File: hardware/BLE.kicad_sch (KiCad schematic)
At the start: 0 parts

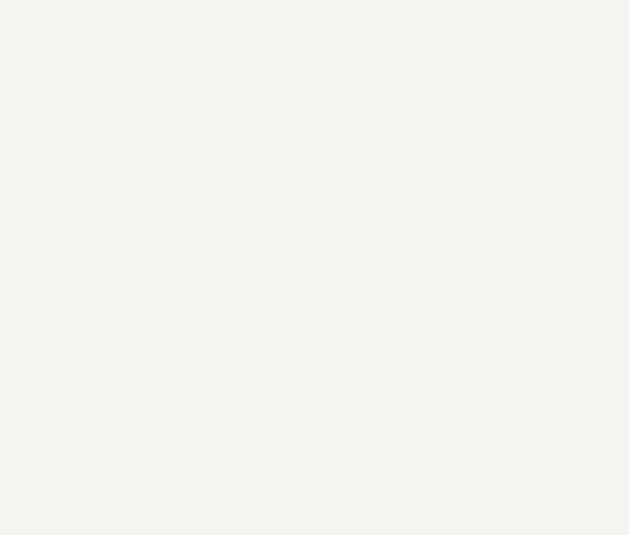
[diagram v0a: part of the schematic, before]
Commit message: Schematic updates: stm32 sheet
Signed-off-by: Connor Rigby <connorr@hey.com>
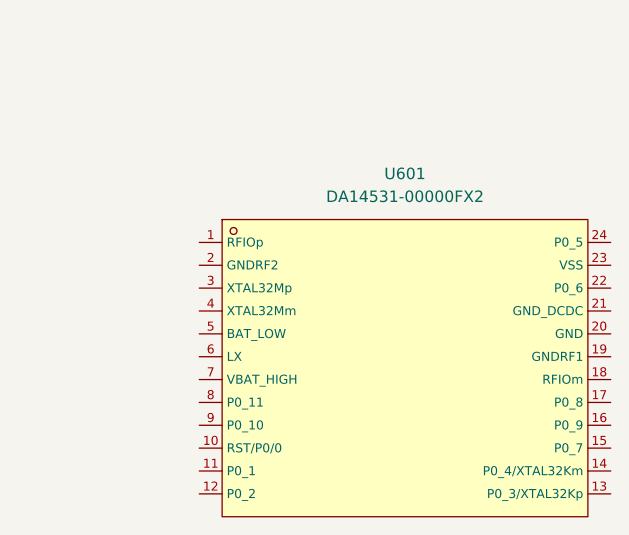
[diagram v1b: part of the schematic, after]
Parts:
- added U601: DA14531-00000FX2, LCSC_Microcontroller:FCGQFN-24_L3.0-W2.2-P0.40-BL, symbol LCSC_Microcontroller:DA14531-00000FX2
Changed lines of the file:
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@@
     (effects (font (size 1.27 1.27)) (justify left))
   )
+  (symbol (lib_id "LCSC_Microcontroller:DA14531-00000FX2") (at 124.46 77.47 0) (unit 1)
+    (in_bom yes) (on_board yes) (fields_autoplaced)
+    (property "Reference" "U601" (id 0) (at 124.46 55.88 0))
+    (property "Value" "DA14531-00000FX2" (id 1) (at 124.46 58.42 0))
+    (property "Footprint" "LCSC_Microcontroller:FCGQFN-24_L3.0-W2.2-P0.40-BL" (id 2) (at 124.46 74.93 0)
+      (effects (font (size 1.27 1.27) italic) hide)
+    )
+    (property "Datasheet" "https://datasheet.lcsc.com/lcsc/2004091707_Dialog-Semiconductor-DA14531-00000FX2_C509077.pdf" (id 3) (at 122.174 64.643 0)
+      (effects (font (size 1.27 1.27)) (justify left) hide)
+    )
+    (property "LCSC" "C509077" (id 4) (at 124.46 64.77 0)
+      (effects (font (size 1.27 1.27)) hide)
+    )
+    (property "MPN" "DA14531-00000FX2" (id 5) (at 124.46 64.77 0)
+      (effects (font (size 1.27 1.27)) hide)
+    )
+    (pin "1")
+    (pin "10")
+    (pin "11")
+    (pin "12")
+    (pin "13")
+    (pin "14")
+    (pin "15")
+    (pin "16")
+    (pin "17")
+    (pin "18")
+    (pin "19")
+    (pin "2")
+    (pin "20")
+    (pin "21")
+    (pin "22")
+    (pin "23")
+    (pin "24")
+    (pin "3")
+    (pin "4")
+    (pin "5")
+    (pin "6")
+    (pin "7")
+    (pin "8")
+    (pin "9")
+  )
 )

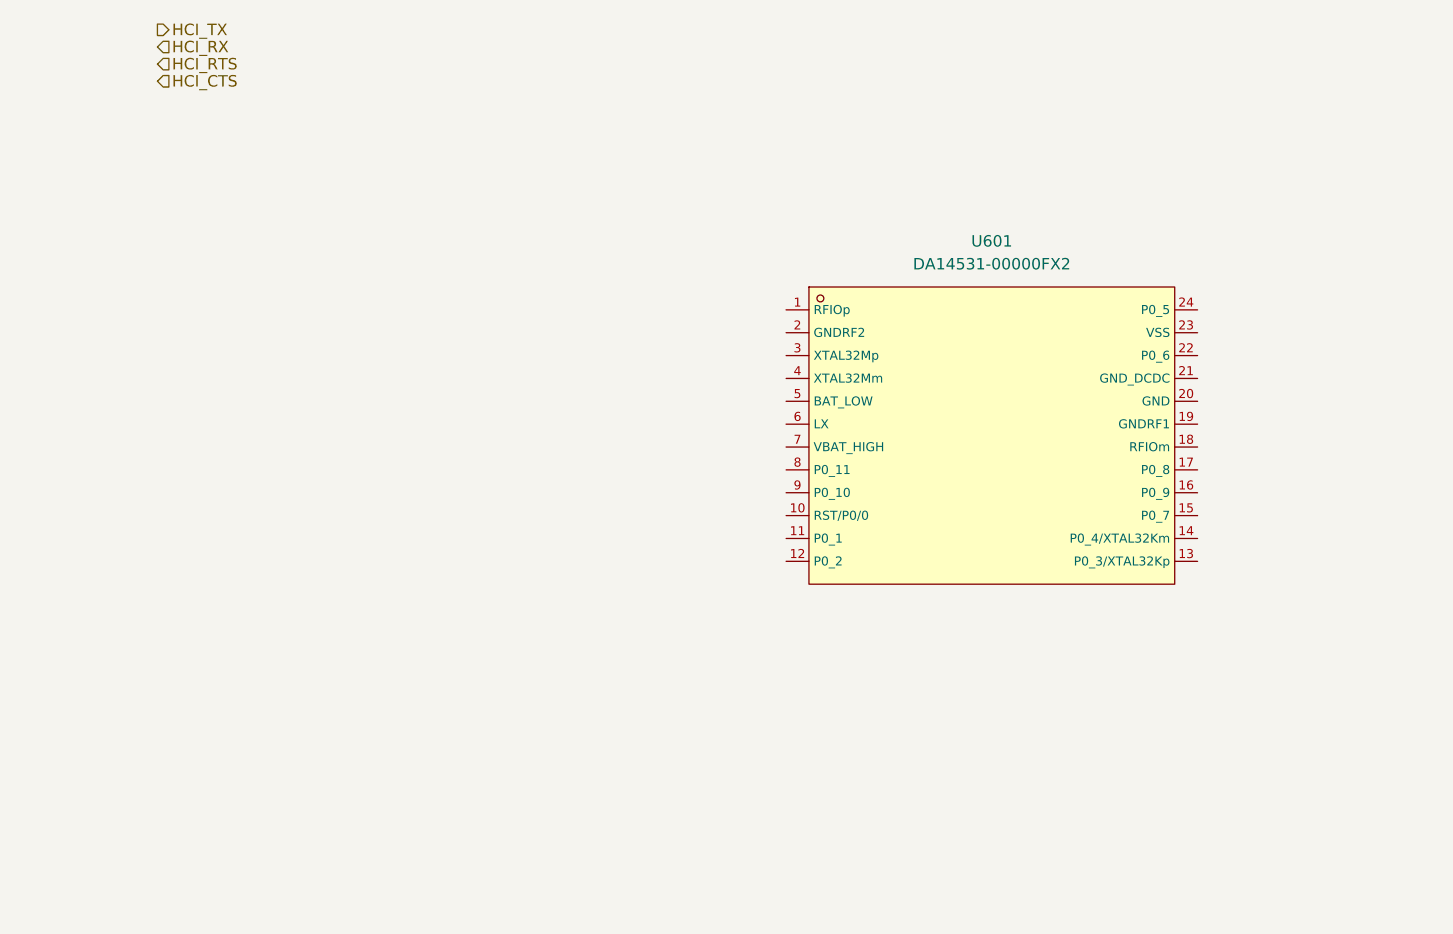
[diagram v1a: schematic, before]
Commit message: Schematic and layout Progress
Signed-off-by: Connor Rigby <connorr@hey.com>
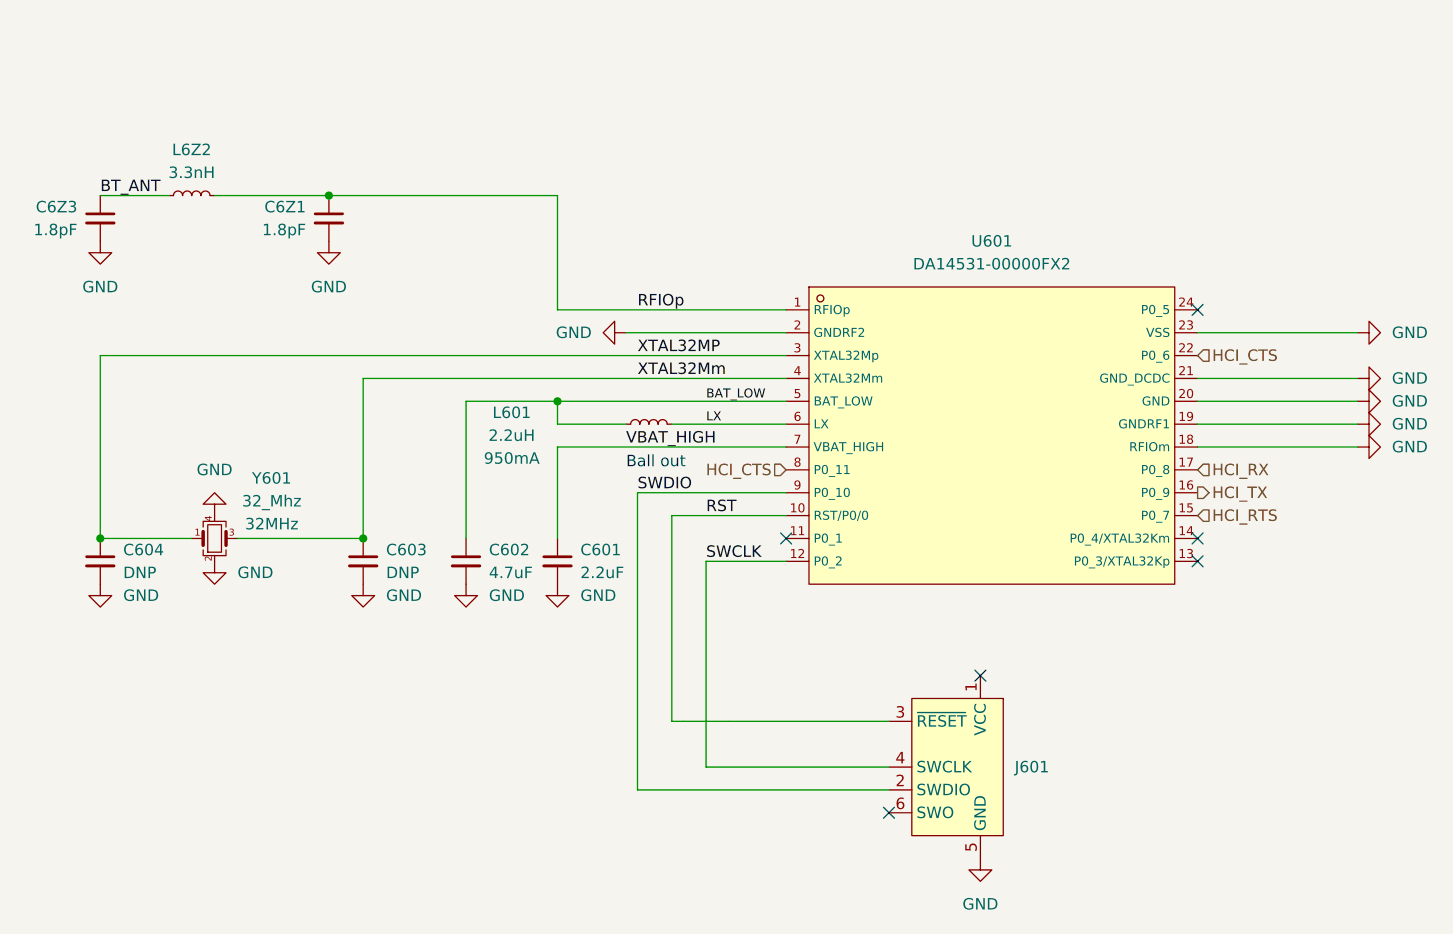
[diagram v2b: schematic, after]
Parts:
- added C601: C_0402_2u2_X75R, Capacitor_SMD:C_0402_1005Metric, symbol LCSC_Capacitor:C_0402_2u2_X75R
- added C602: C_0402_4u7_X5R, Capacitor_SMD:C_0402_1005Metric, symbol LCSC_Capacitor:C_0402_4u7_X5R
- added C603, C604: C_0402_DNP, Capacitor_SMD:C_0402_1005Metric, symbol LCSC_Capacitor:C_0402_DNP
- added C6Z1, C6Z3: C_0402_1p8_C0G, Capacitor_SMD:C_0402_1005Metric, symbol LCSC_Capacitor:C_0402_1p8_C0G
- added J601: Conn_ARM_SWD_TagConnect_TC2030-NL, Connector:Tag-Connect_TC2030-IDC-NL_2x03_P1.27mm_Vertical, symbol Connector:Conn_ARM_SWD_TagConnect_TC2030-NL
- added L601: L_0805_2u2, Inductor_SMD:L_0805_2012Metric, symbol LCSC_Power_Inductor:L_0805_2u2
- added L6Z2: L_0402_3n3, Inductor_SMD:L_0402_1005Metric, symbol LCSC_Inductor:L_0402_3n3
- added Y601: 32_Mhz, Crystal:Crystal_SMD_3225-4Pin_3.2x2.5mm, symbol LCSC_Crystal:32_Mhz
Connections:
- net HCI_CTS: now also U601.22 (P0_6), U601.8 (P0_11)
- net HCI_RTS: now also U601.15 (P0_7)
- net HCI_RX: now also U601.17 (P0_8)
- net HCI_TX: now also U601.16 (P0_9)
- net RFIOp: now reaches U601.1 (RFIOp)
- net RFIOp: now also C6Z1.1, L6Z2.1
- net RST: now reaches U601.10 (RST/P0/0)
- net RST: now also J601.3 (~{RESET})
- net SWCLK: now reaches U601.12 (P0_2)
- net SWCLK: now also J601.4 (SWCLK)
- net GND: now reaches U601.18 (RFIOm)
- net GND: now also U601.19 (GNDRF1), U601.2 (GNDRF2), U601.20 (GND), U601.21 (GND_DCDC), U601.23 (VSS), C601.2, C602.2, C603.2, C604.2, C6Z1.2, C6Z3.2, J601.5 (GND), Y601.2, Y601.4
- net XTAL32MP: now reaches U601.3 (XTAL32Mp)
- net XTAL32MP: now also C604.1, Y601.1
- net XTAL32Mm: now reaches U601.4 (XTAL32Mm)
- net XTAL32Mm: now also C603.1, Y601.3
- net BAT_LOW: now reaches U601.5 (BAT_LOW)
- net BAT_LOW: now also C602.1, L601.1
- net LX: now reaches U601.6 (LX)
- net LX: now also L601.2
- net VBAT_HIGH: now reaches U601.7 (VBAT_HIGH)
- net VBAT_HIGH: now also C601.1
- net SWDIO: now reaches U601.9 (P0_10)
- net SWDIO: now also J601.2 (SWDIO)
- new net BT_ANT: C6Z3.1, L6Z2.2
- no-connect marks 0 -> 6
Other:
- note added: "Ball out"

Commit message: Layout updates
Signed-off-by: Connor Rigby <connorr@hey.com>
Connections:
- net VBAT_HIGH renamed +3.3V
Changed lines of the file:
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@@
   (junction (at 50.8 50.8) (diameter 0) (color 0 0 0 0)
+  )
+  (junction (at 76.2 78.74) (diameter 0) (color 0 0 0 0)
   )
   (junction (at 54.61 88.9) (diameter 0) (color 0 0 0 0)
@@
     (stroke (width 0) (type default))
   )
+  (wire (pts (xy 71.12 78.74) (xy 76.2 78.74))
+    (stroke (width 0) (type default))
+  )
   (wire (pts (xy 85.09 116.84) (xy 113.03 116.84))
     (stroke (width 0) (type default))
@@
   )
   (label "SWDIO" (at 85.09 83.82 0) (fields_autoplaced)
-    (effects (font (size 1.27 1.27)) (justify left bottom))
-  )
-  (label "VBAT_HIGH" (at 83.82 78.74 0) (fields_autoplaced)
     (effects (font (size 1.27 1.27)) (justify left bottom))
   )
@@
   (symbol (lib_id "LCSC_Power_Inductor:L_0805_2u2") (at 86.36 76.2 90) (unit 1)
     (in_bom yes) (on_board yes) (dnp no)
-    (property "Reference" "L601" (at 71.12 74.93 90)
+    (property "Reference" "L601" (at 62.23 74.93 90)
       (effects (font (size 1.27 1.27)))
     )
@@
       (effects (font (size 1.27 1.27)) hide)
     )
-    (property "Inductance" "2.2uH" (at 71.12 77.47 90)
+    (property "Inductance" "2.2uH" (at 62.23 77.47 90)
       (effects (font (size 1.27 1.27)))
     )
@@
       (effects (font (size 1.27 1.27)) hide)
     )
-    (property "Current" "950mA" (at 71.12 80.01 90)
+    (property "Current" "950mA" (at 62.23 80.01 90)
       (effects (font (size 1.27 1.27)))
     )
@@
         )
       )
+    )
+  )
+  (symbol (lib_id "power:+3.3V") (at 71.12 78.74 0) (unit 1)
+    (in_bom yes) (on_board yes) (dnp no) (fields_autoplaced)
+    (property "Reference" "#PWR0601" (at 71.12 82.55 0)
+      (effects (font (size 1.27 1.27)) hide)
+    )
+    (property "Value" "+3.3V" (at 71.12 74.93 0)
+      (effects (font (size 1.27 1.27)))
+    )
+    (property "Footprint" "" (at 71.12 78.74 0)
+      (effects (font (size 1.27 1.27)) hide)
+    )
+    (property "Datasheet" "" (at 71.12 78.74 0)
+      (effects (font (size 1.27 1.27)) hide)
+    )
+    (pin "1")
+    (instances
+      (project "underglow2"
+        (path "/dcbdf88a-d6ac-4b1d-9514-0b0ce113d90b/f6dd0682-1649-403c-b931-941640049f3a"
+          (reference "#PWR0601") (unit 1)
+        )
+      )

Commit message: layout updates
Signed-off-by: Connor Rigby <connorr@hey.com>
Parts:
- added ANT601: BWIPX-1-001E, LCSC_Antenna:IPEX-SMD_BWIPX-1-001E, symbol LCSC_Antenna:BWIPX-1-001E
- added C826, C827: C_0402_DNP, Capacitor_SMD:C_0402_1005Metric, symbol LCSC_Capacitor:C_0402_DNP
- added R804: R_0402_DNP, Resistor_SMD:R_0402_1005Metric, symbol LCSC_Resistor:R_0402_DNP
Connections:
- net BT_ANT: now also C826.2, R804.1
- net GND: now also ANT601.2 (GND), ANT601.3 (GND), C826.1, C827.1
- new net: ANT601.1 (SIG), C827.2, R804.2

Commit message: Almost ready for fab
Signed-off-by: Connor Rigby <connorr@hey.com>
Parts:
- removed C603, C604: C_0402_DNP, Capacitor_SMD:C_0402_1005Metric, symbol LCSC_Capacitor:C_0402_DNP
- removed R804: R_0402_DNP, Resistor_SMD:R_0402_1005Metric, symbol LCSC_Resistor:R_0402_DNP
- added C603, C604: C_0402_33p_C0G, Capacitor_SMD:C_0402_1005Metric, symbol LCSC_Capacitor:C_0402_33p_C0G
- added R601: R_0402_0, Resistor_SMD:R_0402_1005Metric, symbol LCSC_Resistor:R_0402_0
- C826, C827: now not fitted
- J601: now left out of the parts list
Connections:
- net BT_ANT: now also R601.1
- net GND: now also C603.2, C604.2
- net XTAL32MP: now also C604.1
- net XTAL32Mm: now also C603.1
- net BLE_ANT: now reaches ANT601.1 (SIG), C827.2
- net BLE_ANT: now also R601.2

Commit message: Pre-production updates
Signed-off-by: Connor Rigby <connorr@hey.com>
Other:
- note removed: "Ball out"
- company: (none) -> https://cone.codes
- title: (none) -> coneRGB2
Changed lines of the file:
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@@
 (kicad_sch (version 20230121) (generator eeschema)
   (paper "A4")
+  (title_block
+    (title "coneRGB2")
+    (date "2023-03-20")
+    (rev "1")
+    (company "https://cone.codes")
+    (comment 1 "https://github.com/connorrigby/underglow2")
+    (comment 2 "Designed by Connor Rigby")
+    (comment 3 "handles the HCI and lower layers of the BLE stack")
+    (comment 4 "BLE Radio")
+  )
   (junction (at 25.4 50.8) (diameter 0) (color 0 0 0 0)
   )
@@
     (stroke (width 0) (type default))
   )
-  (text "Ball out" (at 83.82 81.28 0)
-    (effects (font (size 1.27 1.27)) (justify left bottom))
+  (text_box "Matching network just in  case.\nNot populated, jumper resistor instead of an inductor."
+    (at 91.44 22.86 0) (size 34.29 7.62)
+    (stroke (width 0) (type default))
+    (fill (type none))
+    (effects (font (size 1.27 1.27)) (justify left top))
+  )
+  (text_box "SWD Required for programming the HCI program and potential debugging"
+    (at 132.08 107.95 0) (size 17.78 13.97)
+    (stroke (width 0) (type default))
+    (fill (type none))
+    (effects (font (size 1.27 1.27)) (justify left top))
   )
   (label "XTAL32Mm" (at 85.09 71.12 0) (fields_autoplaced)

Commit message: Submitted for production
Signed-off-by: Connor Rigby <connorr@hey.com>
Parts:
- added AE602: SMA_Antenna_2.4ghz, Enclosure:SMA_Antenna_Vertical, symbol Device:Antenna
- added AE802: SMA_IPX_Cable, Enclosure:SMA_Connector, symbol Device:Antenna
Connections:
- no-connect marks 6 -> 8
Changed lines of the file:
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@@
   (no_connect (at 101.6 88.9))
   (no_connect (at 147.32 88.9))
+  (no_connect (at 228.6 41.91))
   (no_connect (at 123.19 104.14))
+  (no_connect (at 254 43.18))
   (no_connect (at 147.32 91.44))
   (no_connect (at 147.32 63.5))
@@
   (wire (pts (xy 76.2 50.8) (xy 50.8 50.8))
     (stroke (width 0) (type default))
+  )
+  (rectangle (start 215.9 25.4) (end 266.7 50.8)
+    (stroke (width 0) (type default))
+    (fill (type none))
   )
   (text_box "Matching network just in  case.\nNot populated, jumper resistor instead of an inductor."
@@
         (path "/dcbdf88a-d6ac-4b1d-9514-0b0ce113d90b/f6dd0682-1649-403c-b931-941640049f3a"
           (reference "Y601") (unit 1)
+        )
+      )
+    )
+  )
+  (symbol (lib_id "Device:Antenna") (at 254 38.1 0) (unit 1)
+    (in_bom yes) (on_board no) (dnp no)
+    (property "Reference" "AE802" (at 247.65 30.48 0)
+      (effects (font (size 1.27 1.27)) (justify left))
+    )
+    (property "Value" "SMA_IPX_Cable" (at 247.65 33.02 0)
+      (effects (font (size 1.27 1.27)) (justify left))
+    )
+    (property "Footprint" "Enclosure:SMA_Connector" (at 254 38.1 0)
+      (effects (font (size 1.27 1.27)) hide)
+    )
+    (property "Datasheet" "https://datasheet.lcsc.com/lcsc/2009180306_BAT-WIRELESS-BWIPX1-SMA-1-13L100_C784403.pdf" (at 254 38.1 0)
+      (effects (font (size 1.27 1.27)) hide)
+    )
+    (property "LCSC" "C784403" (at 254 38.1 0)
+      (effects (font (size 1.27 1.27)) hide)
+    )
+    (property "MPN" "BWIPX1-SMA-1.13L100" (at 254 38.1 0)
+      (effects (font (size 1.27 1.27)) hide)
+    )
+    (pin "1")
+    (instances
+      (project "underglow2"
+        (path "/dcbdf88a-d6ac-4b1d-9514-0b0ce113d90b/bab1dc88-b79a-454f-b699-1d1b3e7eefdd"
+          (reference "AE802") (unit 1)
+        )
+        (path "/dcbdf88a-d6ac-4b1d-9514-0b0ce113d90b/f6dd0682-1649-403c-b931-941640049f3a"
+          (reference "AE601") (unit 1)
         )
       )
@@
         )
       )
+    )
+  )
+  (symbol (lib_id "Device:Antenna") (at 228.6 36.83 0) (unit 1)
+    (in_bom yes) (on_board no) (dnp no)
+    (property "Reference" "AE602" (at 224.79 30.48 0)
+      (effects (font (size 1.27 1.27)) (justify left))
+    )
+    (property "Value" "SMA_Antenna_2.4ghz" (at 224.79 33.02 0)
+      (effects (font (size 1.27 1.27)) (justify left))
+    )
+    (property "Footprint" "Enclosure:SMA_Antenna_Vertical" (at 228.6 36.83 0)
+      (effects (font (size 1.27 1.27)) hide)
+    )
+    (property "Datasheet" "https://datasheet.lcsc.com/lcsc/2012241210_HJ-Tech-HJ-2-4GHz-SMA_C1509156.pdf" (at 228.6 36.83 0)
+      (effects (font (size 1.27 1.27)) hide)
+    )
+    (property "LCSC" "C1509156" (at 228.6 36.83 0)
+      (effects (font (size 1.27 1.27)) hide)
+    )
+    (property "MPN" "HJ-2.4GHz-SMA" (at 228.6 36.83 0)
+      (effects (font (size 1.27 1.27)) hide)
+    )
+    (pin "1")
+    (instances
+      (project "underglow2"
+        (path "/dcbdf88a-d6ac-4b1d-9514-0b0ce113d90b/f6dd0682-1649-403c-b931-941640049f3a"
+          (reference "AE602") (unit 1)
+        )
+      )

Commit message: Rev 2 submitted for production
Signed-off-by: Connor Rigby <connorr@hey.com>
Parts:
- removed C601: C_0402_2u2_X75R, Capacitor_SMD:C_0402_1005Metric, symbol LCSC_Capacitor:C_0402_2u2_X75R
- removed C602: C_0402_4u7_X5R, Capacitor_SMD:C_0402_1005Metric, symbol LCSC_Capacitor:C_0402_4u7_X5R
- removed C603, C604: C_0402_33p_C0G, Capacitor_SMD:C_0402_1005Metric, symbol LCSC_Capacitor:C_0402_33p_C0G
- removed J601: Conn_ARM_SWD_TagConnect_TC2030-NL, Connector:Tag-Connect_TC2030-IDC-NL_2x03_P1.27mm_Vertical, symbol Connector:Conn_ARM_SWD_TagConnect_TC2030-NL
- removed L601: L_0805_2u2, Inductor_SMD:L_0805_2012Metric, symbol LCSC_Power_Inductor:L_0805_2u2
- removed U601: DA14531-00000FX2, LCSC_Microcontroller:FCGQFN-24_L3.0-W2.2-P0.40-BL, symbol LCSC_Microcontroller:DA14531-00000FX2
- removed Y601: 32_Mhz, Crystal:Crystal_SMD_3225-4Pin_3.2x2.5mm, symbol LCSC_Crystal:32_Mhz
- added C603: C_0805_1u_X7R, Capacitor_SMD:C_0805_2012Metric, symbol LCSC_Capacitor:C_0805_1u_X7R
- added C604: C_0402_10n_C0G, Capacitor_SMD:C_0402_1005Metric, symbol LCSC_Capacitor:C_0402_10n_X7R
- added C605: C_0805_10u_X5R, Capacitor_SMD:C_0805_2012Metric, symbol LCSC_Capacitor:C_0805_10u_X5R
- added C606, C607, C610, C611, C612: C_0402_100nf_X7R, Capacitor_SMD:C_0402_1005Metric, symbol LCSC_Capacitor:C_0402_100nf_X7R
- added C811 (x4): C_0402_22p_C0G, Capacitor_SMD:C_0402_1005Metric, symbol LCSC_Capacitor:C_0402_22p_C0G
- added J601: Conn_02x03_Odd_Even, Connector:Tag-Connect_TC2030-IDC-NL_2x03_P1.27mm_Vertical, symbol Connector_Generic:Conn_02x03_Odd_Even
- added L601: L_0402_22n, Inductor_SMD:L_0402_1005Metric, symbol LCSC_Inductor:L_0402_22n
- added Q801 (x2): BC817, Package_TO_SOT_SMD:SOT-23, symbol LCSC_Transistor1:BC817
- added R602: R_0603_499, Resistor_SMD:R_0603_1608Metric, symbol LCSC_Resistor:R_0603_499
- added R603, R604, R605, R608: R_0402_10k, Resistor_SMD:R_0402_1005Metric, symbol LCSC_Resistor:R_0402_10k
- added U601: ESP32-C3FH4, LCSC_Microcontroller:QFN50P500X500X90-33N, symbol LCSC_Microcontroller:ESP32-C3FH4
- added Y502: Q13FC1350000400, Crystal:Crystal_SMD_3215-2Pin_3.2x1.5mm, symbol LCSC_Crystal:Q13FC1350000400
- added Y601: 40_Mhz, Crystal:Crystal_SMD_3225-4Pin_3.2x2.5mm, symbol LCSC_Crystal:40_Mhz
- renumbered C6Z3 to C608, C6Z1 to C609, L6Z2 to L602
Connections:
- net GND: now also C603.2, C604.2, C605.2, C606.2, C607.2, C610.2, C611.2, C612.2, C811.1, C811.1, C811.1, C811.1, J601.4 (Pin_4), R608.2, U601.33 (GND), Y601.2, Y601.4
- net HCI_CTS: now also R605.1, U601.14 (GPIO8)
- net HCI_RTS: now also U601.26 (GPIO19)
- net HCI_RX: now also U601.25 (GPIO18)
- net HCI_TX: now also U601.10 (MTDI)
- net RFIOp renamed LNA_IN
- net LNA_IN: now also U601.1 (LNA_IN)
- new net +BATT: C612.1, U601.11 (VDD3P3_RTC)
- new net DTR: Q801.2 (E), R604.1
- new net DTR_1: Q801.1 (B), R604.2
- new net GPIO2: R608.1, U601.6 (GPIO2)
- new net GPIO9: J601.2 (Pin_2), Q801.3 (C), U601.15 (GPIO9)
- new net HCI_EN: J601.5 (Pin_5), Q801.3 (C), U601.7 (CHIP_EN)
- new net RTS: Q801.2 (E), R603.1
- new net RTS_1: Q801.1 (B), R603.2
- new net RXD: J601.3 (Pin_3), U601.27 (U0RXD)
- new net TXD: J601.1 (Pin_1), R602.2
- new net TXD_1: R602.1, U601.28 (U0TXD)
- new net VDD: C603.1, C604.1, C605.1, C606.1, C610.1, C611.1, L601.2, R605.2, U601.17 (VDD3P3_CPU), U601.18 (VDD_SPI), U601.31 (VDDA), U601.32 (VDDA)
- new net VDD3P3: C607.1, L601.1, U601.2 (VDD3P3), U601.3 (VDD3P3)
- new net XTALN: C811.2, U601.29 (XTAL_N), Y601.3
- new net XTALP: C811.2, U601.30 (XTAL_P), Y601.1
- new net XTAL_32K_N: C811.2, U601.5 (XTAL_32K_N), Y502.1
- new net XTAL_32K_P: C811.2, U601.4 (XTAL_32K_P), Y502.2
- no-connect marks 8 -> 14
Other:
- moved on the sheet: AE602, AE802, L602
